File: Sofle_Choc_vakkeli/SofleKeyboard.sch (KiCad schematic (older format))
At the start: 96 parts, among them J2 4PIN, J3 OLED, P1 i2c_pin, P2 i2c_pin, SW1 SW_PUSH_LED, SW10 SW_PUSH_LED, SW11 SW_PUSH_LED, SW12 SW_PUSH_LED, SW13 SW_PUSH_LED, SW14 SW_PUSH_LED, SW15 SW_PUSH_LED, SW16 SW_PUSH_LED, SW17 SW_PUSH_LED, SW18 SW_PUSH_LED, SW19 SW_PUSH_LED, SW2 SW_PUSH_LED, SW20 SW_PUSH_LED, SW21 SW_PUSH_LED, SW22 SW_PUSH_LED, SW23 SW_PUSH_LED, SW24 SW_PUSH_LED, SW25 Rotary_Encoder_Switch, SW26 SW_PUSH_LED, SW27 SW_PUSH_LED, SW28 SW_PUSH_LED, SW29 SW_PUSH_LED, SW3 SW_PUSH_LED, SW30 SW_PUSH_LED, SW31 SW_PUSH_LED, SW32 SW_PUSH_LED, SW33 SW_PUSH_LED, SW34 SW_PUSH_LED, SW35 SW_PUSH_LED, SW4 SW_PUSH_LED, SW5 SW_PUSH_LED, SW6 SW_PUSH_LED, SW7 SW_PUSH_LED, SW8 SW_PUSH_LED, SW9 SW_PUSH_LED, U1 ProMicro

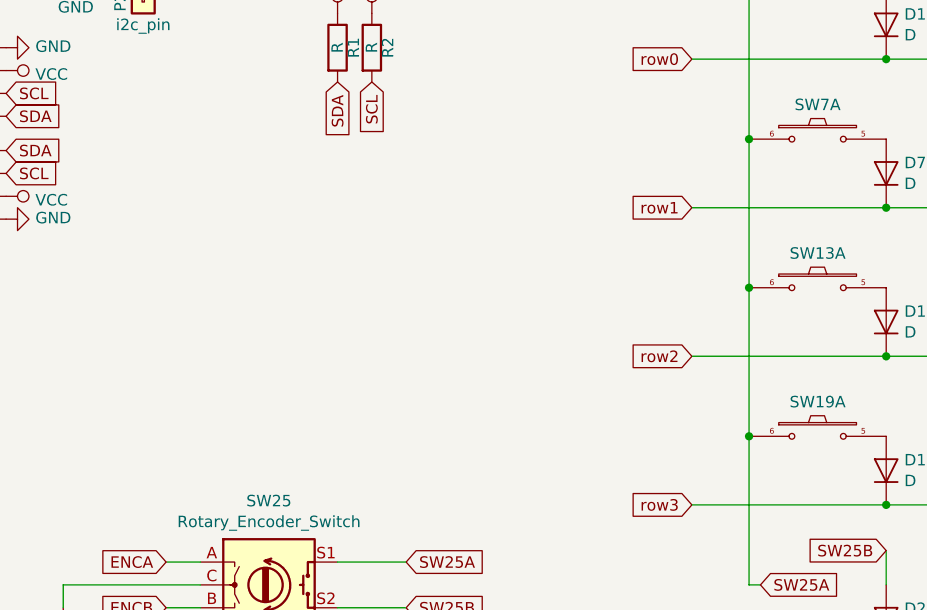
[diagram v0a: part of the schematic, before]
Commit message: fixed single breakable button gnd, added dxf for 3d.
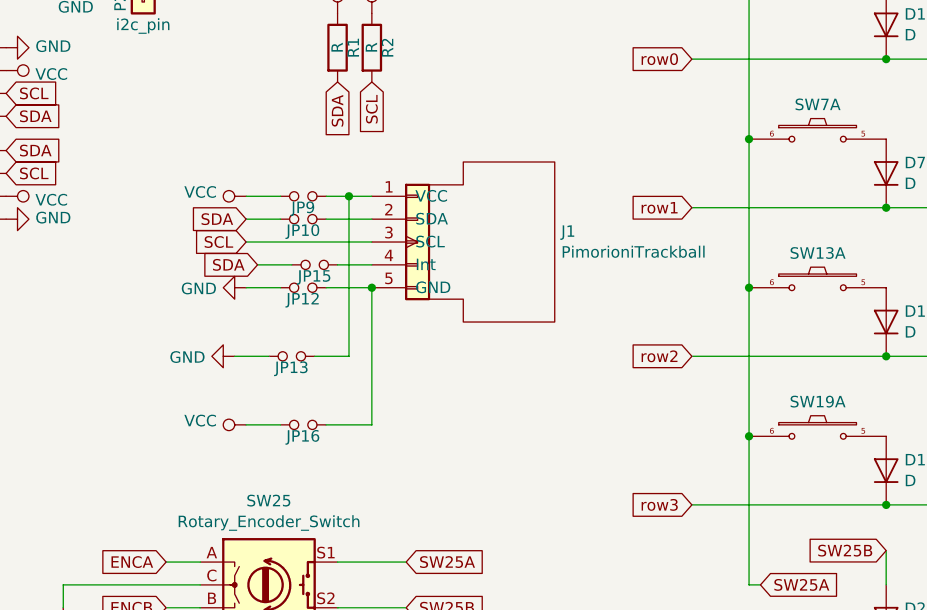
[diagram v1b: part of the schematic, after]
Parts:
- added J1: PimorioniTrackball, Keebio-Parts:pimoroni_trackball, symbol SofleKeyboard:PimorioniTrackball
- added JP10, JP12, JP13, JP15, JP16, JP9: Jumper_NO_Small, SofleKeyboard-footprint:Jumper, symbol SofleKeyboard-rescue:Jumper_NO_Small-Device
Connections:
- net GND: now also JP12.1, JP13.1
- net SCL: now also J1.3 (SCL)
- net SDA: now also JP10.1, JP15.1
- net VCC: now also JP16.1, JP9.1
- new net: J1.1 (VCC), JP13.2, JP9.2
- new net: J1.2 (SDA), JP10.2
- new net: J1.4 (Int), JP15.2
- new net: J1.5 (GND), JP12.2, JP16.2

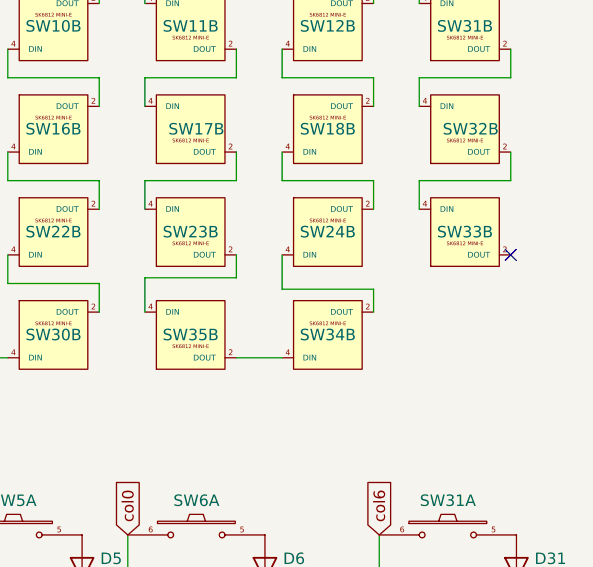
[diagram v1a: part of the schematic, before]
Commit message: fixed single button led order
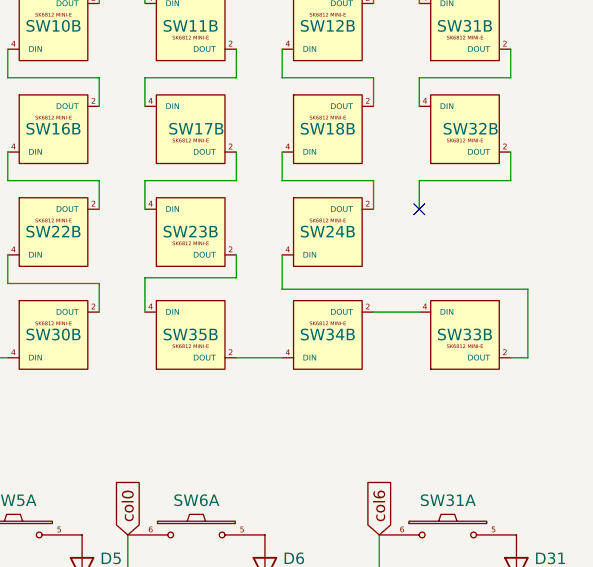
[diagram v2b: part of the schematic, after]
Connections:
- net at SW24.4 (DIN): now also SW33.2 (DOUT); no longer SW34.2 (DOUT)
- net at SW33.4 (DIN): now also SW34.2 (DOUT); no longer SW32.2 (DOUT)
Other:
- moved on the sheet: SW33B
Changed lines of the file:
@@
 L SofleKeyboard:SW_PUSH_LED SW33
 U 2 1 61F8202C
-P 10125 2225
-F 0 "SW33" H 10125 2225 50  0000 C CNN
-F 1 "SW_PUSH_LED" H 10125 2499 50  0001 C CNN
-F 2 "SofleChoc:Choc_Hotswap_SK6812MiniE" H 10125 2475 50  0001 C CNN
-F 3 "" H 10125 2475 50  0001 C CNN
-	2    10125 2225
+P 10125 2675
+F 0 "SW33" H 10125 2675 50  0000 C CNN
+F 1 "SW_PUSH_LED" H 10125 2949 50  0001 C CNN
+F 2 "SofleChoc:Choc_Hotswap_SK6812MiniE" H 10125 2925 50  0001 C CNN
+F 3 "" H 10125 2925 50  0001 C CNN
+	2    10125 2675
 	-1   0    0    -1
 $EndComp
@@
 	8725 2425 8725 2575
 Wire Wire Line
-	9725 2575 9725 2475
-Wire Wire Line
-	9725 2475 9325 2475
-Wire Wire Line
 	9325 2475 9325 2325
 Wire Wire Line
@@
 Wire Wire Line
 	9925 775  9925 1225
-NoConn ~ 10325 2325
+NoConn ~ 9925 2125
 $Comp
 L SofleKeyboard-rescue:D-Lily58-cache-Lily58_Pro-rescue D31
@@
 Wire Wire Line
 	2450 4450 2600 4450
+Wire Wire Line
+	9725 2575 9925 2575
+Wire Wire Line
+	10325 2775 10400 2775
+Wire Wire Line
+	10400 2775 10400 2475
+Wire Wire Line
+	10400 2475 9325 2475
 $EndSCHEMATC
